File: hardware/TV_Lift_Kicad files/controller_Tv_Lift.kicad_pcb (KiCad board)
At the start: 4 copper layers, 70 x 157.5 mm, 97 parts, among them J1 socket LAN8720a, J10 CONN_IR_OUT, J11 1844223, J12 C5360899, J2 1836189, J3 1844223, J4 1844210, J5 1844223, J6 1844223, J7 1844236, J8 C5360899, J9 1844210, Q2 MMBT3906, SW1 UP, SW2 DOWN, SW3 STOP, SW4 Reset, U1 MAX3232, U10 VNH5019A-E, U2 TSOP32S40F, U3 SN65HVD230, U4 ESP32-WROOM-32, U5 LM2596S-5, U6 AMS1117-3.3, U7 PC817, U8 PC817, U9 b0505s-1we

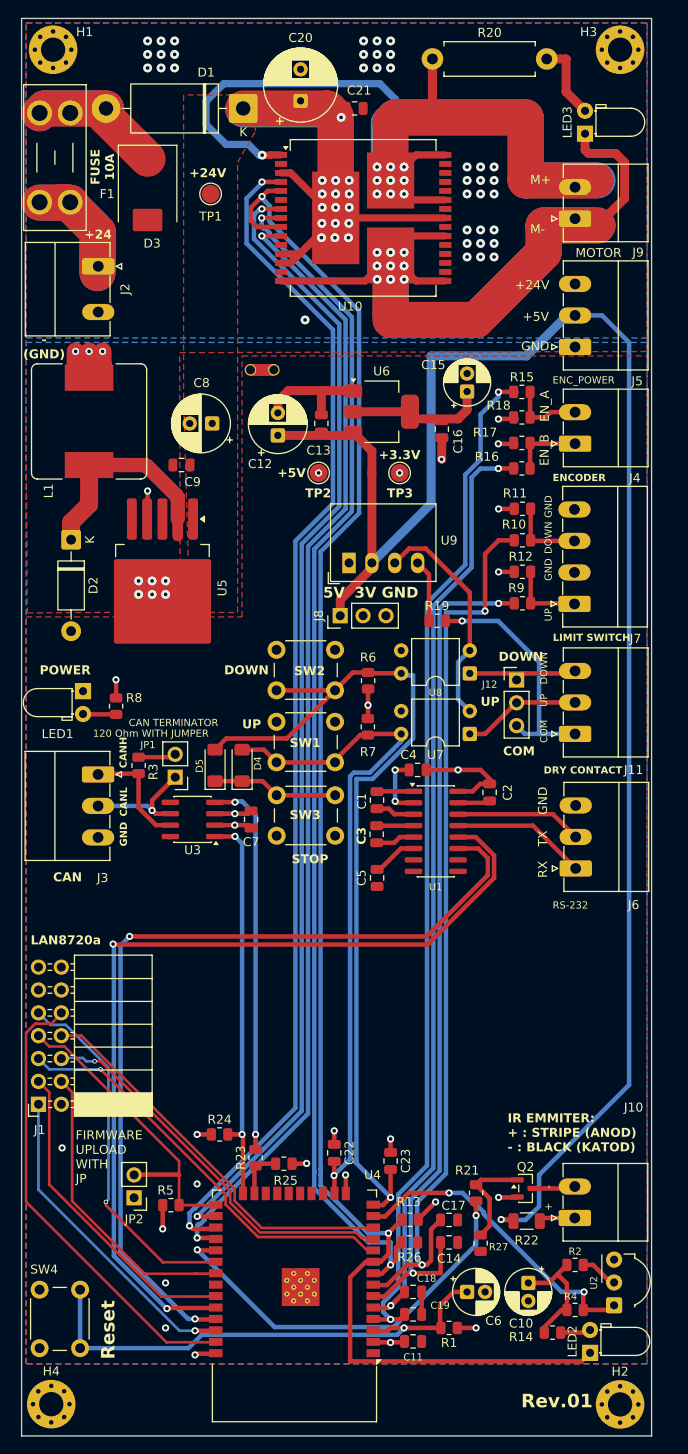
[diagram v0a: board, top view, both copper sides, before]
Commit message: fix input manager: correct limit switch logic and remove unnecessary comments
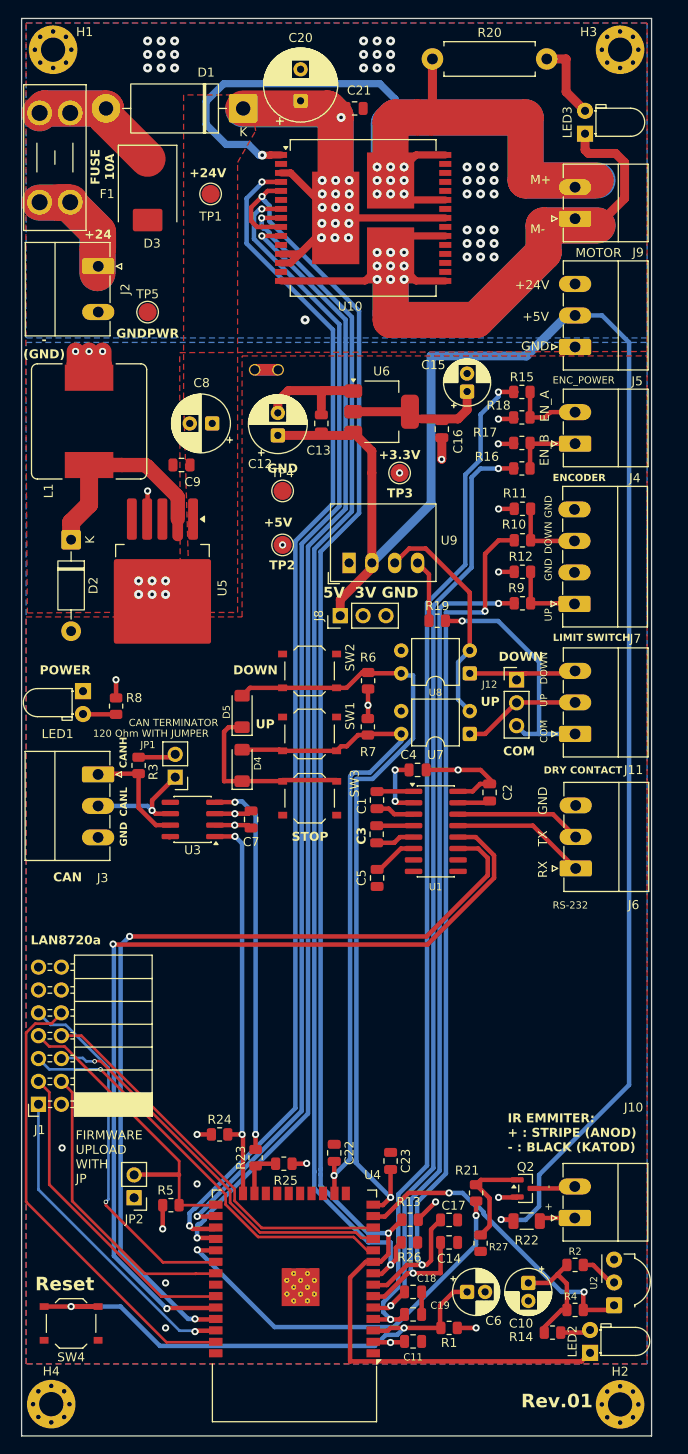
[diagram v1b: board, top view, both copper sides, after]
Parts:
- added TP4: Signal GND, TestPoint:TestPoint_Pad_D2.0mm, F.Cu at (94.5, 78.0)
- added TP5: GNDPWR, TestPoint:TestPoint_Pad_D2.0mm, F.Cu at (79.5, 58.1)
- C14, C17: value 100 nF 16V -> 100 nF 50V
- C18, C19: value 1 nF 16V -> 1 nF 50V
- J10: value CONN_IR_OUT -> 1844210
- SW1: value UP -> TS-1187A-BAB; footprint Button_Switch_THT:SW_PUSH_6mm -> Button_Switch_SMD:SW_Push_1P1T_XKB_TS-1187A
- SW2: value DOWN -> TS-1187A-BAB; footprint Button_Switch_THT:SW_PUSH_6mm -> Button_Switch_SMD:SW_Push_1P1T_XKB_TS-1187A
- SW3: value STOP -> TS-1187A-BAB; footprint Button_Switch_THT:SW_PUSH_6mm -> Button_Switch_SMD:SW_Push_1P1T_XKB_TS-1187A
- SW4: value Reset -> TS-1187A-BAB; footprint Button_Switch_THT:SW_PUSH_6mm -> Button_Switch_SMD:SW_Push_1P1T_XKB_TS-1187A
- moved TP2 8.94 mm to (94.5, 84.0)
- moved D5 6.71 mm to (90.0, 102.5)
- moved SW3 5.04 mm to (97.5, 112.1)
- moved SW4 4.45 mm to (71.0, 170.5), turned to 180 degrees
- moved SW2 4.36 mm to (97.5, 98.0)
- moved SW1 3.91 mm to (97.5, 105.0)
- moved NT2 0.47 mm to (94.0, 64.5)
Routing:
- net /DRY_CONTACT_DOWN: track 100.9 -> 89.0 mm
- net GND: track 36.6 -> 29.3 mm, vias 11 -> 7
- net Net-(D4-K): track 14.0 -> 20.3 mm
- net Net-(U4-EN): track 57.2 -> 62.5 mm, vias 1 -> 2
- net /DRY_CONTACT_UP: track 76.7 -> 75.3 mm
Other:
- board text added: "GNDPWR"

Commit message: change capacitors on smd
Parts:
- removed LED3: LED_Dual_Bidirectional_GREEN_BLUE, LED_THT:LED_D3.0mm_Horizontal_O1.27mm_Z6.0mm
- added C24: 1 nF 50V, Capacitor_SMD:C_0805_2012Metric, F.Cu at (108.7, 162.7)
- added C25: C7171, Capacitor_Tantalum_SMD:CP_EIA-3216-18_Kemet-A, F.Cu at (110.6, 173.8)
- added D6: KT-0805W, LED_SMD:LED_0805_2012Metric, F.Cu at (131.1, 35.0)
- added D7: KT-0805G, LED_SMD:LED_0805_2012Metric, F.Cu at (131.1, 38.0)
- C10: value 10 uF 10V -> C19702; footprint Capacitor_THT:CP_Radial_D5.0mm_P2.00mm -> Capacitor_SMD:C_0603_1608Metric
- C11: value 100 nF 16V -> 100 nF 50V
- C6: value 10 uF 16V -> C7171; footprint Capacitor_THT:CP_Radial_D5.0mm_P2.00mm -> Capacitor_Tantalum_SMD:CP_EIA-3216-18_Kemet-A
- LED1: value LED_GREEN_F3 -> KT-0805Y; footprint LED_THT:LED_D3.0mm_Horizontal_O1.27mm_Z2.0mm -> LED_SMD:LED_0805_2012Metric
- LED2: value LED_RED_F3 -> NCD0805R1; footprint LED_THT:LED_D3.0mm_Horizontal_O1.27mm_Z6.0mm -> LED_SMD:LED_0805_2012Metric
- moved R1 4.69 mm to (116.1, 167.5), turned to -90 degrees
- moved C10 4.06 mm to (125.0, 163.5), turned to 180 degrees
- moved R8 3.69 mm to (74.6, 98.5), turned to 180 degrees
- moved LED2 3.11 mm to (131.5, 172.5)
- moved LED1 2.91 mm to (70.0, 98.5), turned to 0 degrees
- moved R2 2.83 mm to (125.0, 166.0), turned to 0 degrees
- moved R4 2.06 mm to (125.0, 168.5)
- moved C6 1.50 mm to (113.5, 167.0), turned to 90 degrees
- moved C11 1.41 mm to (110.0, 171.5)
- moved C19 1.35 mm to (110.0, 168.6)
- moved C18 1.21 mm to (110.0, 166.3)
- moved R26 1.17 mm to (108.7, 160.3)
- moved R13 0.98 mm to (108.7, 158.0)
- moved R14 0.51 mm to (125.0, 171.5)
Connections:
- C10 pad 1: +3.3V -> Net-(U2-Vs)
- R2 pad 1: Net-(U2-Vs) -> +3.3V
- R2 pad 2: +3.3V -> Net-(U2-Vs)
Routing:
- net GND: track 29.3 -> 3.19 mm, vias 7 -> 4
- net Net-(D6-A): track 8.79 -> 14.7 mm
- net /M1_DIAG: track 181.2 -> 185.1 mm, vias 2 -> 4
- net +3.3V: track 72.4 -> 76.1 mm, vias 15 -> 16
- net Net-(U2-Vs): track 4.62 -> 8.19 mm
- net Net-(D6-K): track 150.7 -> 147.2 mm
- net Net-(LED2-A): track 3.38 -> 5.61 mm
- net Net-(U4-EN): track 62.5 -> 60.2 mm
- net Net-(LED1-A): track 3.69 -> 2.74 mm
- net /M1_LIMIT_UP: track 96.1 -> 97.0 mm
- net /IR_BLASTER: track 45.2 -> 44.5 mm
- net /ENC_A: track 114.4 -> 115.0 mm
- net /ENC_B: track 105.4 -> 106.0 mm
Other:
- board text added: "MOTOR ERROR"
